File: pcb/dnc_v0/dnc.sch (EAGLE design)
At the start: 67 parts, among them IC1 74HC595D, IC2 74HC595D, Q1 200mA/50V, Q2 TSM2306CX, Q3 TSM2306CX, Q4 TSM2306CX, Q5 TSM2306CX, Q6 200mA/50V, Q7 TSM2306CX, Q8 TSM2306CX

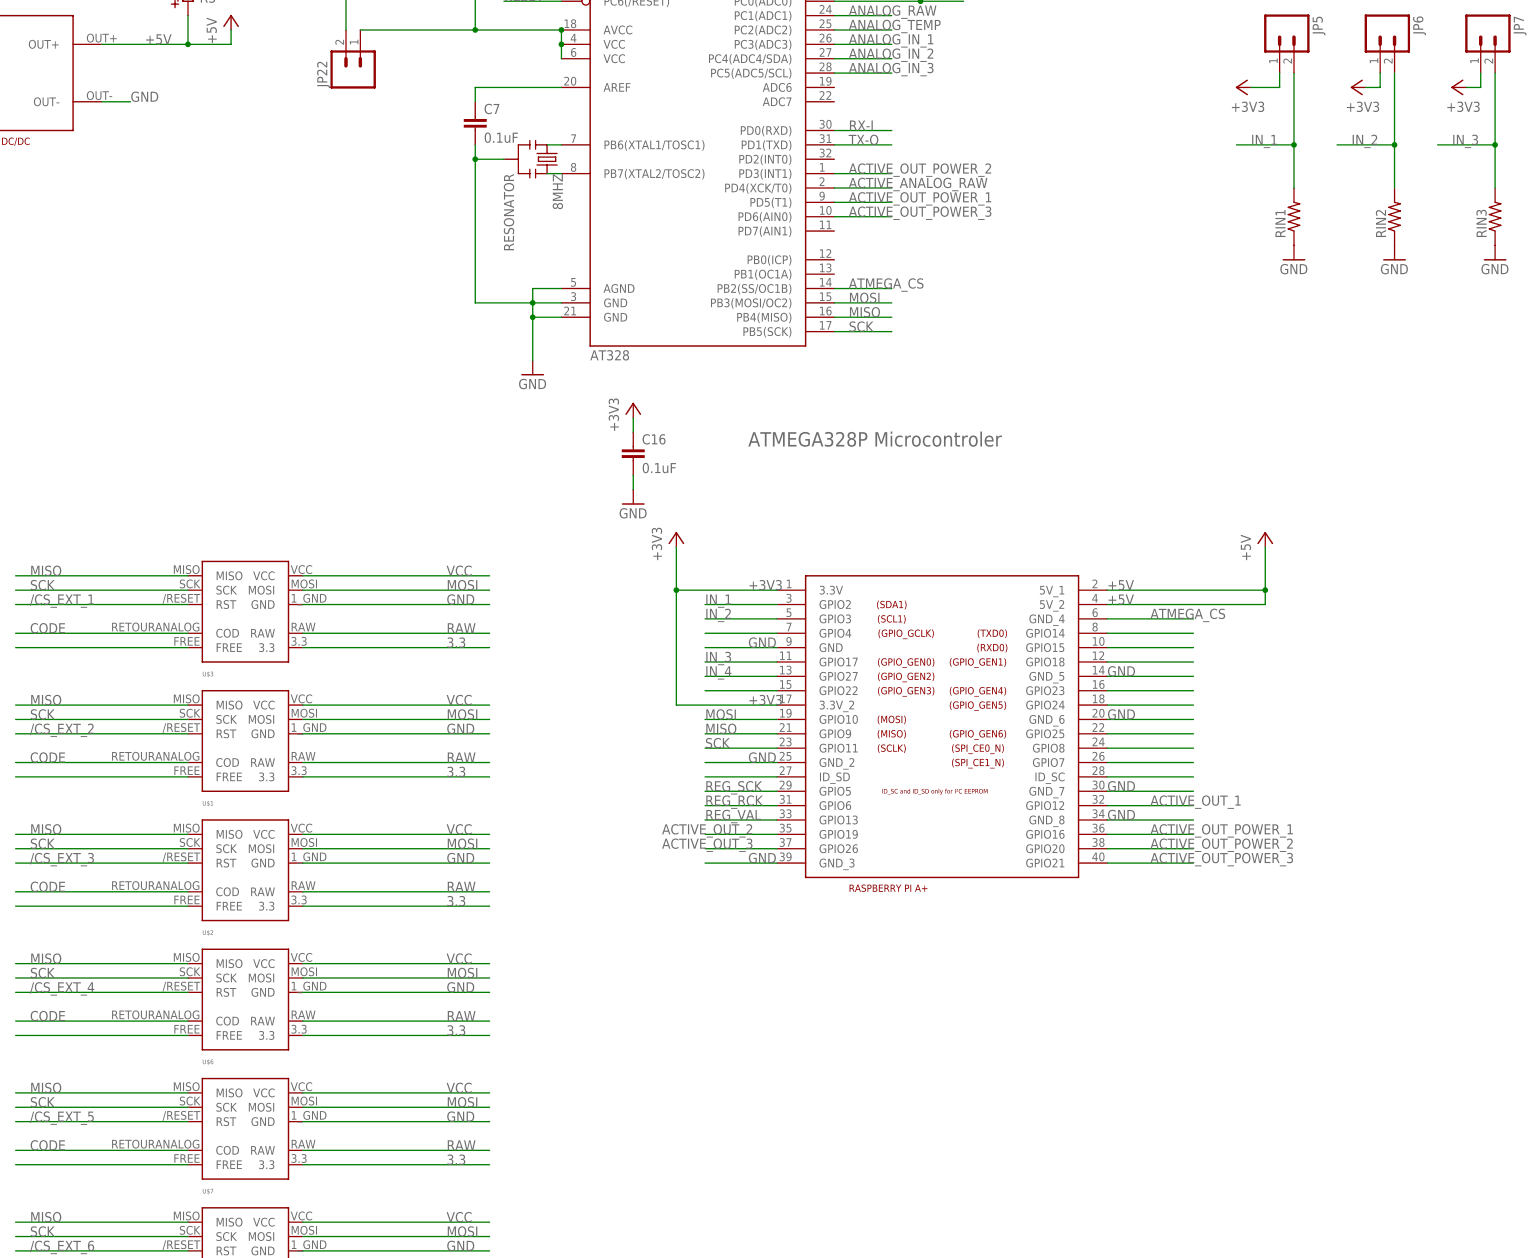
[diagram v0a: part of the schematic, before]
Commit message: Clean dnc_v0 directory
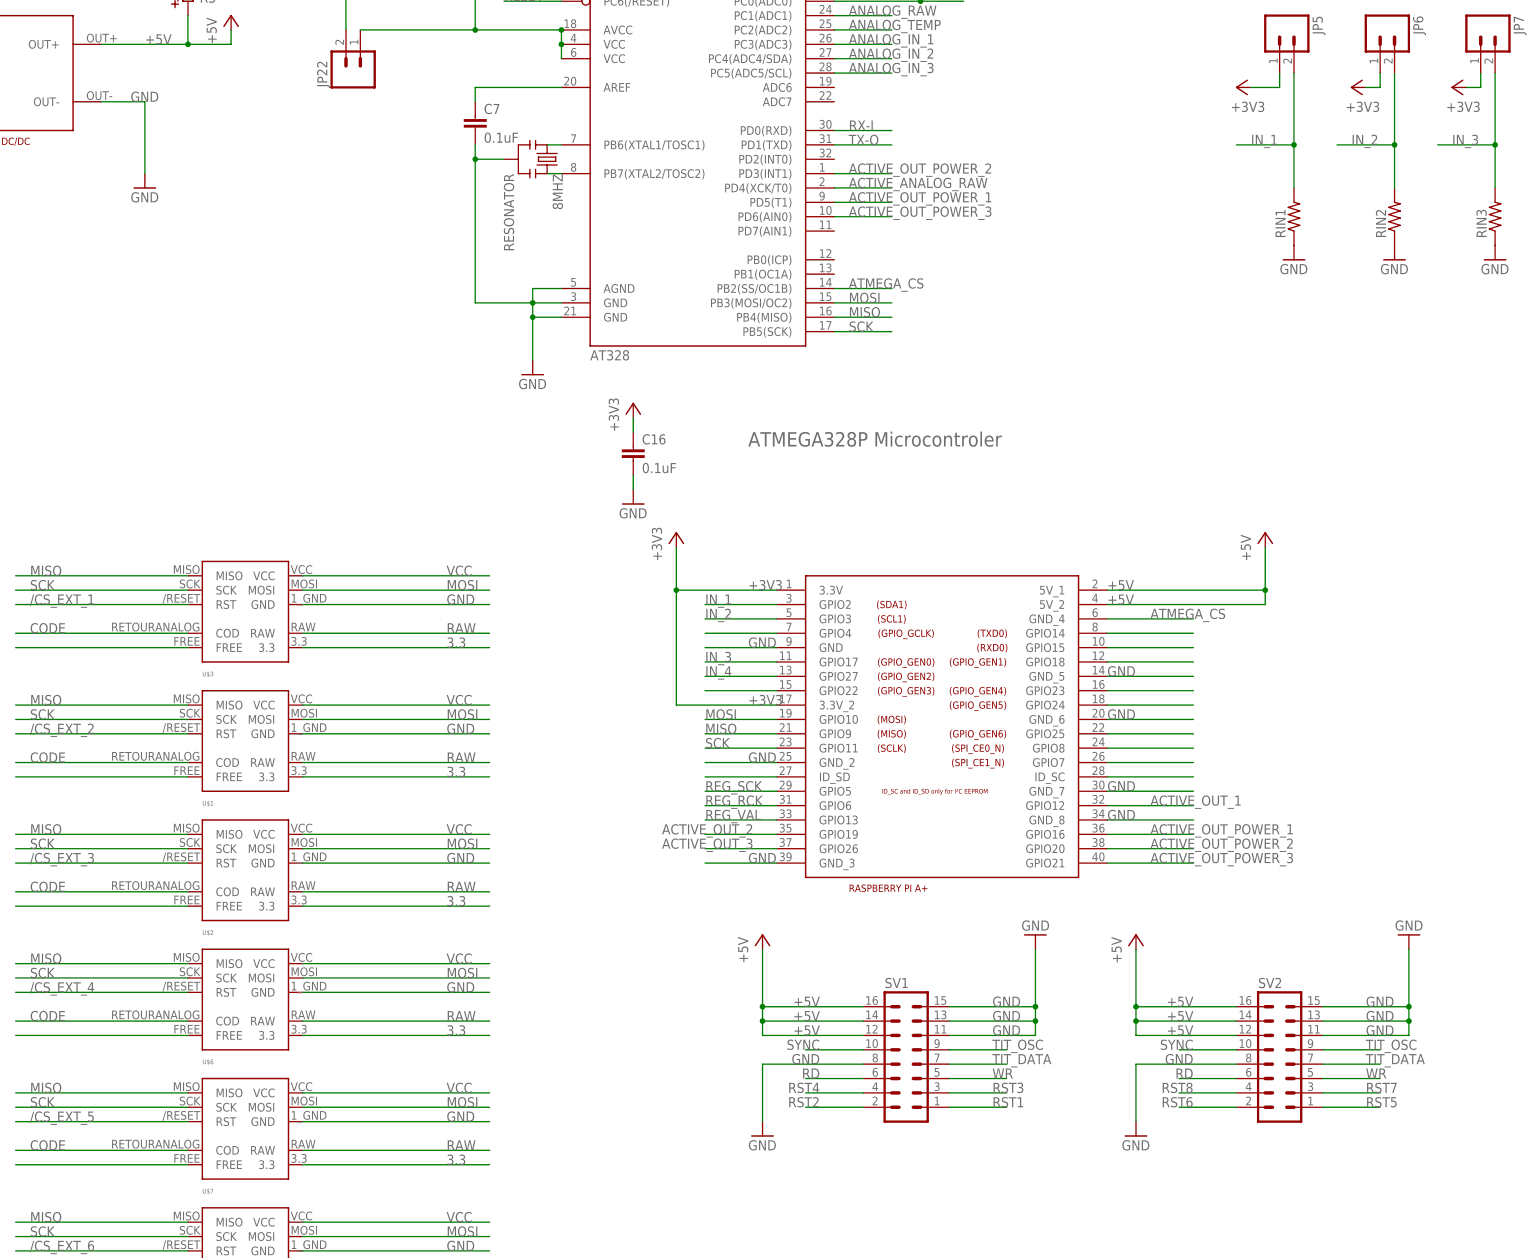
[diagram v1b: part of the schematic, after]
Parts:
- added SV1, SV2: (no value), con-lstb:MA08-2
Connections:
- new net RD: SV1.6, SV2.6
- new net SYNC: SV1.10, SV2.10
- new net TIT_DATA: SV1.7, SV2.7
- new net TIT_OSC: SV1.9, SV2.9
- new net WR: SV1.5, SV2.5
- net +5V: now also SV1.12, SV1.14, SV1.16, SV2.12, SV2.14, SV2.16
- net GND: now also SV1.11, SV1.13, SV1.15, SV1.8, SV2.11, SV2.13, SV2.15, SV2.8
- net RST1: now also SV1.1
- net RST2: now also SV1.2
- net RST3: now also SV1.3
- net RST4: now also SV1.4
- net RST5: now also SV2.1
- net RST6: now also SV2.2
- net RST7: now also SV2.3
- net RST8: now also SV2.4

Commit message: Correct some big mistackes on schematics, and lib
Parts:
- removed U$1, U$2, U$3, U$6, U$7, U$8: EXT-DNC, pierre_vv:EXT-DNC
- added A+_UART: (no value), SparkFun:M02LOCK_LONGPADS
- added EXT1, EXT2, EXT3, EXT4, EXT5, EXT6: EXT-DNC, pierre_vv:EXT-DNC
- renumbered IC1 to REG1, IC2 to REG2, JP1 to RAW_IN, JP10 to PWR_OUT2, JP11 to PWR_OUT3, JP12 to JP_OUT1, JP2 to A_IN1, JP20 to JP_OUT2, JP21 to JP_OUT3, JP22 to 3.3/5, JP3 to A_IN2, JP4 to A_IN3, JP5 to IN1, JP6 to IN2, JP7 to IN3, JP8 to IN4, JP9 to PWR_OUT1, Q1 to MOS_BAT, Q2 to MOS_PWR2, Q3 to MOS_PWR1, Q4 to MOS_PWR3, Q6 to MOS_TEMP, SV1 to TITREUR1, SV2 to TITREUR2
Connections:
- removed net 3.3: U$1.3.3, U$2.3.3, U$3.3.3, U$6.3.3, U$7.3.3, U$8.3.3
- removed net N$31: U$4.GPIO14
- removed net N$32: U$4.GPIO15
- removed net N$33: U$4.GPIO18
- removed net N$34: U$4.GPIO23
- removed net VCC: U$1.VCC, U$2.VCC, U$3.VCC, U$6.VCC, U$7.VCC, U$8.VCC
- new net RXA+: A+_UART.2, U$4.GPIO15
- new net TXA+: A+_UART.1, U$4.GPIO14
- net +3V3: now also EXT1.3.3V, EXT2.3.3V, EXT3.3.3V, EXT4.3.3V, EXT5.3.3V, EXT6.3.3V
- net +5V: now also EXT1.5V, EXT2.5V, EXT3.5V, EXT4.5V, EXT5.5V, EXT6.5V; no longer MOS_PWR1.D, MOS_PWR2.D, MOS_PWR3.D
- net /CS_EXT_1: now also EXT1.RST; no longer U$3.RST
- net /CS_EXT_2: now also EXT2.RST; no longer U$1.RST
- net /CS_EXT_3: now also EXT3.RST; no longer U$2.RST
- net /CS_EXT_4: now also EXT4.RST; no longer U$6.RST
- net /CS_EXT_5: now also EXT5.RST; no longer U$7.RST
- net /CS_EXT_6: now also EXT6.RST; no longer U$8.RST
- net ACTIVE_OUT_POWER_1: no longer U$4.GPIO16
- net ACTIVE_OUT_POWER_2: no longer U$4.GPIO20
- net ACTIVE_OUT_POWER_3: no longer U$4.GPIO21
- net CODE: now also EXT1.COD, EXT2.COD, EXT3.COD, EXT4.COD, EXT5.COD, EXT6.COD; no longer U$1.COD, U$2.COD, U$3.COD, U$6.COD, U$7.COD, U$8.COD
- net GND: now also EXT1.GND, EXT2.GND, EXT3.GND, EXT4.GND, EXT5.GND, EXT6.GND; no longer U$1.GND, U$2.GND, U$3.GND, U$6.GND, U$7.GND, U$8.GND
- net MISO: now also EXT1.MISO, EXT2.MISO, EXT3.MISO, EXT4.MISO, EXT5.MISO, EXT6.MISO; no longer U$1.MISO, U$2.MISO, U$3.MISO, U$6.MISO, U$7.MISO, U$8.MISO
- net MOSI: now also EXT1.MOSI, EXT2.MOSI, EXT3.MOSI, EXT4.MOSI, EXT5.MOSI, EXT6.MOSI; no longer U$1.MOSI, U$2.MOSI, U$3.MOSI, U$6.MOSI, U$7.MOSI, U$8.MOSI
- net N$10: now also EXT6.FREE; no longer U$8.FREE
- net N$21: now also EXT1.FREE; no longer U$3.FREE
- net N$4: now also EXT2.FREE; no longer U$1.FREE
- net N$5: now also EXT3.FREE; no longer U$2.FREE
- net N$8: now also EXT4.FREE; no longer U$6.FREE
- net N$9: now also EXT5.FREE; no longer U$7.FREE
- net RAW: now also EXT1.RAW, EXT2.RAW, EXT3.RAW, EXT4.RAW, EXT5.RAW, EXT6.RAW, MOS_PWR1.D, MOS_PWR2.D, MOS_PWR3.D; no longer U$1.RAW, U$2.RAW, U$3.RAW, U$6.RAW, U$7.RAW, U$8.RAW
- net SCK: now also EXT1.SCK, EXT2.SCK, EXT3.SCK, EXT4.SCK, EXT5.SCK, EXT6.SCK; no longer U$1.SCK, U$2.SCK, U$3.SCK, U$6.SCK, U$7.SCK, U$8.SCK

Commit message: New brd far better, but not finished
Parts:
- renumbered C1 to CRST, C16 to C3.3, C7 to CMHZ, R1 to RBAT1, R2 to RBAT2, R26 to RRST, R3 to RTEMP1, R4 to RTEMP2, R5 to RTEMP0, R8 to RBAT0, RIN5 to ROUT1, RIN6 to ROUT2, RIN7 to ROUT3
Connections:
- removed net N$15: U$4.GPIO4
- removed net N$18: U$4.GPIO22
- removed net N$23: U$4.ID_SD
- removed net N$35: U$4.GPIO24
- removed net N$36: U$4.GPIO25
- removed net N$37: U$4.GPIO8
- removed net N$38: U$4.GPIO7
- removed net N$39: U$4.ID_SC
- new net ANALOG_BAT: AT328.PC1(ADC1)
- net +3V3: now also U$4.GPIO24
- net /CS_EXT_1: now also U$4.GPIO7
- net /CS_EXT_2: now also U$4.GPIO5
- net /CS_EXT_3: now also U$4.GPIO4
- net /CS_EXT_4: now also U$4.GPIO3
- net /CS_EXT_5: now also U$4.GPIO2
- net /CS_EXT_6: now also U$4.GND_4
- net ACTIVE_OUT_1: now also U$4.GPIO16; no longer U$4.GPIO12
- net ACTIVE_OUT_2: now also U$4.GPIO20; no longer U$4.GPIO19
- net ACTIVE_OUT_3: now also U$4.GPIO21; no longer U$4.GPIO26
- net ANALOG_IN_1: now also AT328.PC3(ADC3)
- net ANALOG_IN_2: now also AT328.PC4(ADC4/SDA)
- net ANALOG_IN_3: now also AT328.PC5(ADC5/SCL)
- net ANALOG_TEMP: now also AT328.PC2(ADC2)
- net ATMEGA_CS: now also U$4.GPIO23; no longer U$4.GND_4
- net CODE: now also AT328.PC0(ADC0)
- net IN_1: now also U$4.GPIO26; no longer U$4.GPIO2
- net IN_2: now also U$4.GPIO19; no longer U$4.GPIO3
- net IN_3: now also U$4.GPIO13; no longer U$4.GPIO17
- net IN_4: now also U$4.GPIO6; no longer U$4.GPIO27
- net REG_RCK: now also U$4.GPIO17; no longer U$4.GPIO6
- net REG_SCK: now also U$4.GPIO22; no longer U$4.GPIO5
- net REG_VAL: now also U$4.GPIO27; no longer U$4.GPIO13
- net RX-I: now also AT328.PD0(RXD)
- net TX-O: now also AT328.PD1(TXD)
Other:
- moved on the sheet: EXT5, EXT6

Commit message: Manual brd just before GND
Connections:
- removed net RD: TITREUR1.6, TITREUR2.6
- removed net REG_SCK: REG1A.SCK, REG2A.SCK, U$4.GPIO22
- removed net REG_VAL: REG1A.SER, U$4.GPIO27
- removed net SYNC: TITREUR1.10, TITREUR2.10
- removed net TIT_DATA: TITREUR1.7, TITREUR2.7
- removed net TIT_OSC: TITREUR1.9, TITREUR2.9
- removed net WR: TITREUR1.5, TITREUR2.5
- net ACTIVE_OUT_POWER_1: now also AT328.PD2(INT0)
- net MOSI: now also REG1A.SER, TITREUR1.7, TITREUR2.7
- net SCK: now also REG1A.SCK, REG2A.SCK, TITREUR1.5, TITREUR2.5
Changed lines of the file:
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@@
 <pinref part="ISP1" gate="G$1" pin="4"/>
+</segment>
+<segment>
+<pinref part="REG1" gate="A" pin="SER"/>
+<wire x1="-157.48" y1="2.54" x2="-172.72" y2="2.54" width="0.1524" layer="91"/>
+<label x="-172.72" y="2.54" size="1.778" layer="95"/>
+</segment>
+<segment>
+<pinref part="TITREUR1" gate="G$1" pin="7"/>
+<wire x1="88.9" y1="-83.82" x2="99.06" y2="-83.82" width="0.1524" layer="91"/>
+<label x="96.52" y="-83.82" size="1.778" layer="95"/>
+</segment>
+<segment>
+<pinref part="TITREUR2" gate="G$1" pin="7"/>
+<wire x1="154.94" y1="-83.82" x2="165.1" y2="-83.82" width="0.1524" layer="91"/>
+<label x="162.56" y="-83.82" size="1.778" layer="95"/>
 </segment>
 </net>
@@
 <wire x1="-71.12" y1="-63.5" x2="-101.6" y2="-63.5" width="0.1524" layer="91"/>
 <label x="-99.06" y="-63.5" size="1.778" layer="95"/>
+</segment>
+<segment>
+<pinref part="REG2" gate="A" pin="SCK"/>
+<wire x1="-177.8" y1="-43.18" x2="-157.48" y2="-43.18" width="0.1524" layer="91"/>
+<pinref part="REG1" gate="A" pin="SCK"/>
+<wire x1="-157.48" y1="-2.54" x2="-177.8" y2="-2.54" width="0.1524" layer="91"/>
+<wire x1="-177.8" y1="-2.54" x2="-193.04" y2="-2.54" width="0.1524" layer="91"/>
+<wire x1="-177.8" y1="-2.54" x2="-177.8" y2="-43.18" width="0.1524" layer="91"/>
+<junction x="-177.8" y="-2.54"/>
+<label x="-193.04" y="-2.54" size="1.778" layer="95"/>
+</segment>
+<segment>
+<pinref part="TITREUR1" gate="G$1" pin="5"/>
+<wire x1="88.9" y1="-86.36" x2="99.06" y2="-86.36" width="0.1524" layer="91"/>
+<label x="96.52" y="-86.36" size="1.778" layer="95"/>
+</segment>
+<segment>
+<pinref part="TITREUR2" gate="G$1" pin="5"/>
+<wire x1="154.94" y1="-86.36" x2="165.1" y2="-86.36" width="0.1524" layer="91"/>
+<label x="162.56" y="-86.36" size="1.778" layer="95"/>
 </segment>
 </net>
@@
 <wire x1="139.7" y1="-88.9" x2="129.54" y2="-88.9" width="0.1524" layer="91"/>
 <label x="132.08" y="-88.9" size="1.778" layer="95" rot="MR0"/>
-</segment>
-</net>
-<net name="REG_VAL" class="0">
-<segment>
-<pinref part="REG1" gate="A" pin="SER"/>
-<wire x1="-157.48" y1="2.54" x2="-172.72" y2="2.54" width="0.1524" layer="91"/>
-<label x="-172.72" y="2.54" size="1.778" layer="95"/>
-</segment>
-<segment>
-<pinref part="U$4" gate="G$1" pin="GPIO27"/>
-<wire x1="58.42" y1="-15.24" x2="45.72" y2="-15.24" width="0.1524" layer="91"/>
-<label x="45.72" y="-15.24" size="1.778" layer="95"/>
 </segment>
 </net>
@@
 </segment>
 </net>
-<net name="REG_SCK" class="0">
-<segment>
-<pinref part="REG1" gate="A" pin="SCK"/>
-<wire x1="-157.48" y1="-2.54" x2="-177.8" y2="-2.54" width="0.1524" layer="91"/>
-<pinref part="REG2" gate="A" pin="SCK"/>
-<wire x1="-177.8" y1="-2.54" x2="-193.04" y2="-2.54" width="0.1524" layer="91"/>
-<wire x1="-177.8" y1="-2.54" x2="-177.8" y2="-43.18" width="0.1524" layer="91"/>
-<wire x1="-177.8" y1="-43.18" x2="-157.48" y2="-43.18" width="0.1524" layer="91"/>
-<junction x="-177.8" y="-2.54"/>
-<label x="-193.04" y="-2.54" size="1.778" layer="95"/>
-</segment>
-<segment>
-<pinref part="U$4" gate="G$1" pin="GPIO22"/>
-<wire x1="58.42" y1="-17.78" x2="45.72" y2="-17.78" width="0.1524" layer="91"/>
-<label x="45.72" y="-17.78" size="1.778" layer="95"/>
-</segment>
-</net>
 <net name="REG_RCK" class="0">
 <segment>
@@
 <wire x1="254" y1="106.68" x2="254" y2="91.44" width="0.1524" layer="91"/>
 <pinref part="PWR_OUT1" gate="G$1" pin="1"/>
-</segment>
-</net>
-<net name="ACTIVE_OUT_POWER_1" class="0">
-<segment>
-<pinref part="MOS_PWR1" gate="G$1" pin="G"/>
-<wire x1="246.38" y1="111.76" x2="238.76" y2="111.76" width="0.1524" layer="91"/>
-<label x="220.98" y="111.76" size="1.778" layer="95"/>
-<pinref part="ROUT1" gate="G$1" pin="2"/>
-<wire x1="238.76" y1="111.76" x2="233.68" y2="111.76" width="0.1524" layer="91"/>
-<wire x1="238.76" y1="96.52" x2="238.76" y2="111.76" width="0.1524" layer="91"/>
-<junction x="238.76" y="111.76"/>
-</segment>
-<segment>
-<wire x1="68.58" y1="68.58" x2="78.74" y2="68.58" width="0.1524" layer="91"/>
-<label x="71.12" y="68.58" size="1.778" layer="95"/>
 </segment>
 </net>
@@
 </segment>
 </net>
-<net name="WR" class="0">
-<segment>
-<pinref part="TITREUR1" gate="G$1" pin="5"/>
-<wire x1="88.9" y1="-86.36" x2="99.06" y2="-86.36" width="0.1524" layer="91"/>
-<label x="96.52" y="-86.36" size="1.778" layer="95"/>
-</segment>
-<segment>
-<pinref part="TITREUR2" gate="G$1" pin="5"/>
-<wire x1="154.94" y1="-86.36" x2="165.1" y2="-86.36" width="0.1524" layer="91"/>
-<label x="162.56" y="-86.36" size="1.778" layer="95"/>
-</segment>
-</net>
-<net name="RD" class="0">
-<segment>
-<pinref part="TITREUR1" gate="G$1" pin="6"/>
-<wire x1="73.66" y1="-86.36" x2="63.5" y2="-86.36" width="0.1524" layer="91"/>
-<label x="66.04" y="-86.36" size="1.778" layer="95" rot="MR0"/>
-</segment>
-<segment>
-<pinref part="TITREUR2" gate="G$1" pin="6"/>
-<wire x1="139.7" y1="-86.36" x2="129.54" y2="-86.36" width="0.1524" layer="91"/>
-<label x="132.08" y="-86.36" size="1.778" layer="95" rot="MR0"/>
-</segment>
-</net>
-<net name="TIT_DATA" class="0">
-<segment>
-<pinref part="TITREUR1" gate="G$1" pin="7"/>
-<wire x1="88.9" y1="-83.82" x2="99.06" y2="-83.82" width="0.1524" layer="91"/>
-<label x="96.52" y="-83.82" size="1.778" layer="95"/>
-</segment>
-<segment>
-<pinref part="TITREUR2" gate="G$1" pin="7"/>
-<wire x1="154.94" y1="-83.82" x2="165.1" y2="-83.82" width="0.1524" layer="91"/>
-<label x="162.56" y="-83.82" size="1.778" layer="95"/>
-</segment>
-</net>
-<net name="TIT_OSC" class="0">
-<segment>
-<pinref part="TITREUR1" gate="G$1" pin="9"/>
-<wire x1="88.9" y1="-81.28" x2="99.06" y2="-81.28" width="0.1524" layer="91"/>
-<label x="96.52" y="-81.28" size="1.778" layer="95"/>
-</segment>
-<segment>
-<pinref part="TITREUR2" gate="G$1" pin="9"/>
-<wire x1="154.94" y1="-81.28" x2="165.1" y2="-81.28" width="0.1524" layer="91"/>
-<label x="162.56" y="-81.28" size="1.778" layer="95"/>
-</segment>
-</net>
-<net name="SYNC" class="0">
-<segment>
-<pinref part="TITREUR1" gate="G$1" pin="10"/>
-<wire x1="73.66" y1="-81.28" x2="63.5" y2="-81.28" width="0.1524" layer="91"/>
-<label x="66.04" y="-81.28" size="1.778" layer="95" rot="MR0"/>
-</segment>
-<segment>
-<pinref part="TITREUR2" gate="G$1" pin="10"/>
-<wire x1="139.7" y1="-81.28" x2="129.54" y2="-81.28" width="0.1524" layer="91"/>
-<label x="132.08" y="-81.28" size="1.778" layer="95" rot="MR0"/>
-</segment>
-</net>
 <net name="ANALOG_BAT" class="0">
 <segment>
@@
 </segment>
 </net>
+<net name="ACTIVE_OUT_POWER_1" class="0">
+<segment>
+<pinref part="ROUT1" gate="G$1" pin="2"/>
+<wire x1="238.76" y1="96.52" x2="238.76" y2="111.76" width="0.1524" layer="91"/>
+<pinref part="MOS_PWR1" gate="G$1" pin="G"/>
+<wire x1="238.76" y1="111.76" x2="246.38" y2="111.76" width="0.1524" layer="91"/>
+<wire x1="238.76" y1="111.76" x2="228.6" y2="111.76" width="0.1524" layer="91"/>
+<junction x="238.76" y="111.76"/>
+<label x="218.44" y="111.76" size="1.778" layer="95"/>
+</segment>
+<segment>
+<pinref part="AT328" gate="G$1" pin="PD2(INT0)"/>
+<wire x1="68.58" y1="76.2" x2="78.74" y2="76.2" width="0.1524" layer="91"/>
+<label x="71.12" y="76.2" size="1.778" layer="95"/>
+</segment>
+</net>

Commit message: Place labels
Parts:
- renumbered ISP1 to ISP, JP_OUT1 to OUT1, JP_OUT2 to OUT2, JP_OUT3 to OUT3, RTEMP1 to PTC
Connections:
- new net REG_CLR: REG1A.SCL, REG2A.SCL, U$4.GPIO27
- net +3V3: no longer REG1A.SCL, REG2A.SCL
- net /CS_EXT_1: now also U$4.GPIO12; no longer U$4.GPIO7
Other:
- moved on the sheet: REG1, REG2

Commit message: Update lib and clean up the brd
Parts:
- A_IN1, A_IN2, A_IN3: value (none) -> DNC_IN3; device SparkFun:M03LOCK_LONGPADS -> pierre_vv:DNC_IN3
- IN1, IN2, IN3, IN4: value (none) -> DNC_IN2; device SparkFun:M02LOCK_LONGPADS -> pierre_vv:DNC_IN2
- OUT1, OUT2, OUT3: value M02LOCK_LONGPADS -> DNC_IN2; device SparkFun-Connectors:M02LOCK_LONGPADS -> pierre_vv:DNC_IN2
- PWR_OUT1, PWR_OUT2, PWR_OUT3, RAW_IN: value M025MM -> DNC_IN2PWR; device SparkFun-Connectors:M025MM -> pierre_vv:DNC_IN2PWR
- TITREUR1, TITREUR2: value (none) -> DNC_TITREUR; device con-lstb:MA08-2 -> pierre_vv:DNC_TITREUR

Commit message: Finished brd before first print
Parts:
- removed JP15, JP16, JP17, JP18: STAND-OFF, SparkFun:STAND-OFF
- F1: value PTC0603 -> PTCPTH; device SparkFun-PowerIC:PTC0603 -> SparkFun-PowerIC:PTCPTH
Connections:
- net ACTIVE_ANALOG_RAW: now also AT328.PD4(XCK/T0)
- net ATMEGA_CS: now also AT328.PB2(SS/OC1B)
- net MISO: now also AT328.PB4(MISO)
- net MOSI: now also AT328.PB3(MOSI/OC2)
- net SCK: now also AT328.PB5(SCK)
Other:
- moved on the sheet: 3.3/5, 8MHZ, A+_UART, AT328, A_IN1, A_IN2, A_IN3, C2, C3.3, CMHZ, CRST, EXT1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
